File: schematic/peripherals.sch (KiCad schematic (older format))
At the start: 5 parts, among them U501 24LC16B

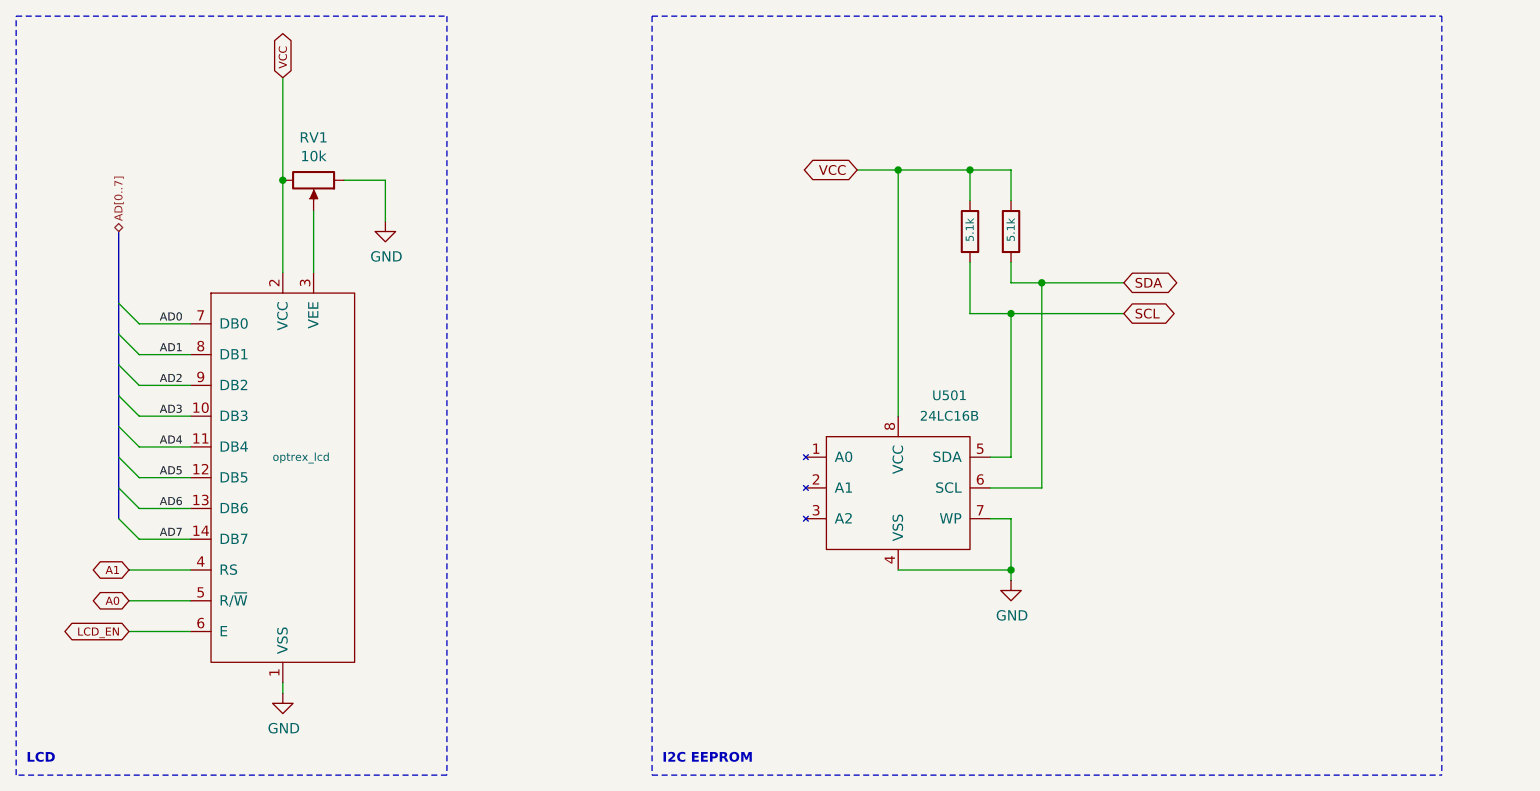
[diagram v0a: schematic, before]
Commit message: [L4] Add I/O expander to schematic
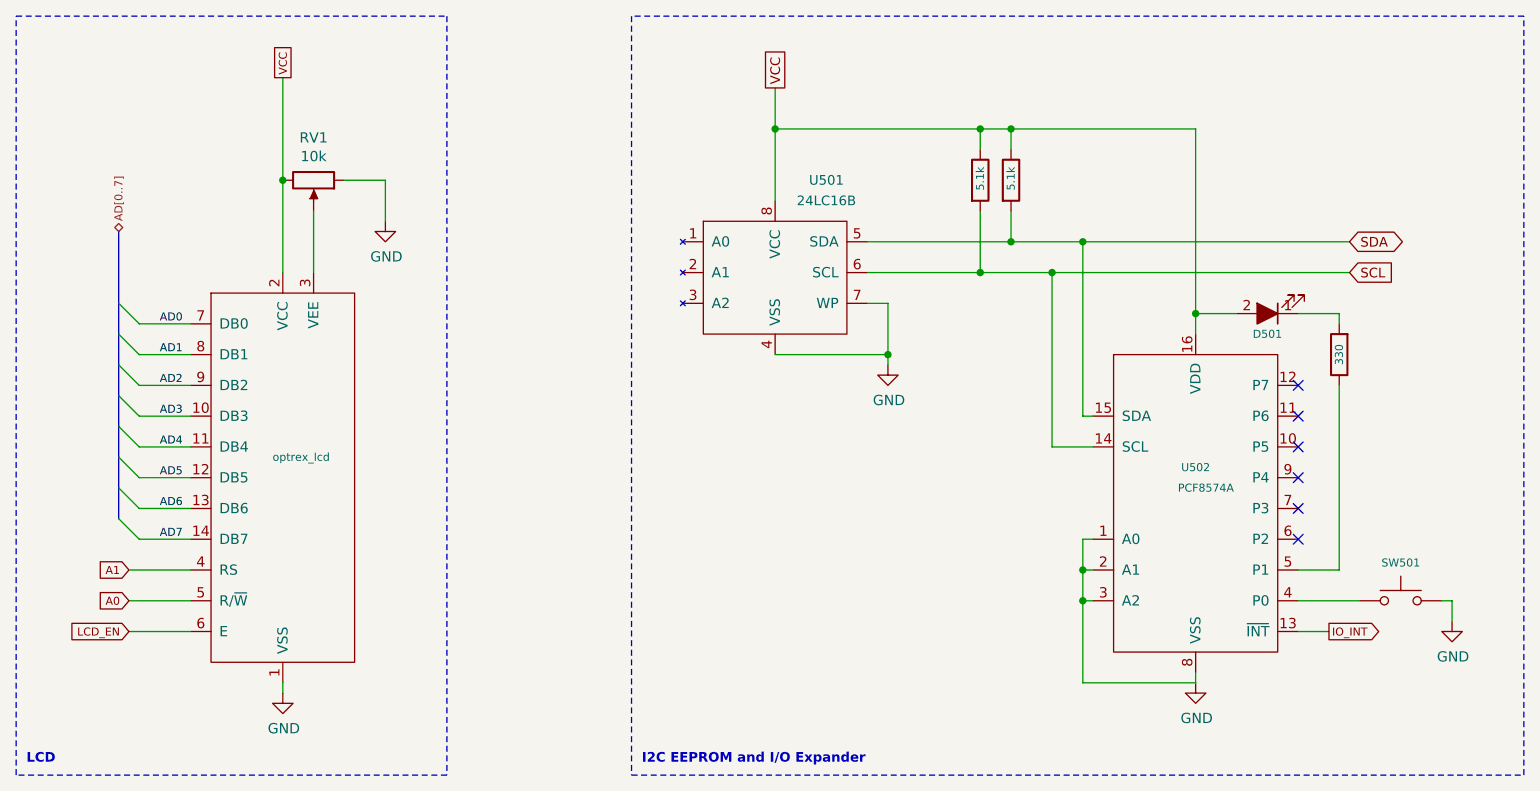
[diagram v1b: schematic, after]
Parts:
- added D501: LED_ALT, symbol LED_ALT
- added R?: 330, symbol R
- added SW501: SW_Push, symbol SW_Push
- added U502: PCF8574A, symbol PCF8574A
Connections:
- net GND: now also SW501.2, U502.1 (A0), U502.2 (A1), U502.3 (A2), U502.8 (VSS)
- net SCL: now also U501.6 (SCL), U502.14 (SCL); no longer U501.5 (SDA)
- net SDA: now also U501.5 (SDA), U502.15 (SDA); no longer U501.6 (SCL)
- net VCC: now also D501.2 (A), U502.16 (VDD)
- new net: SW501.1, U502.4 (P0)
- new net: R?.1, U502.5 (P1)
- new net: D501.1 (K), R?.2
- new net IO_INT: U502.13 (~INT)
- no-connect marks 0 -> 6
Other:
- note added: "I2C EEPROM and I/O Expander"
- note removed: "I2C EEPROM"
- moved on the sheet: U501
